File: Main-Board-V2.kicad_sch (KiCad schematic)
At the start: 12 parts, among them IC1 REG1117-5, J4 1-776163-5, U1 OPA325IDBVR, U2 Teensy4.0

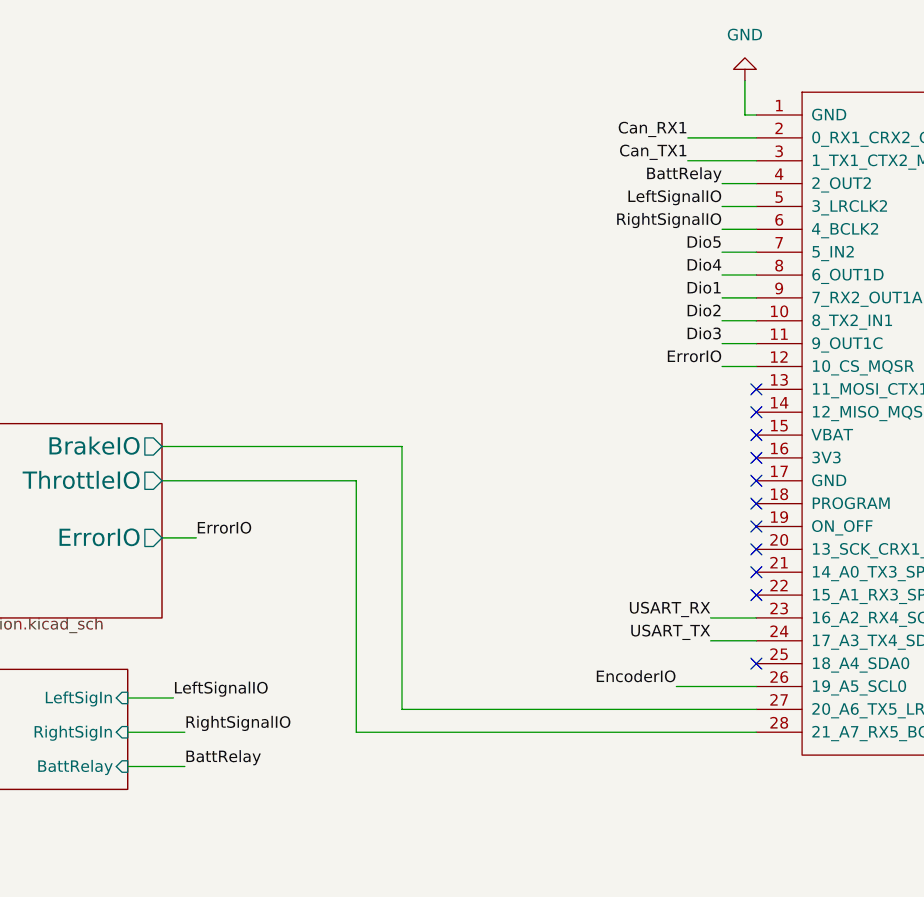
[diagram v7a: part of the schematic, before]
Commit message: finished re-routing, only silkscreen errors left
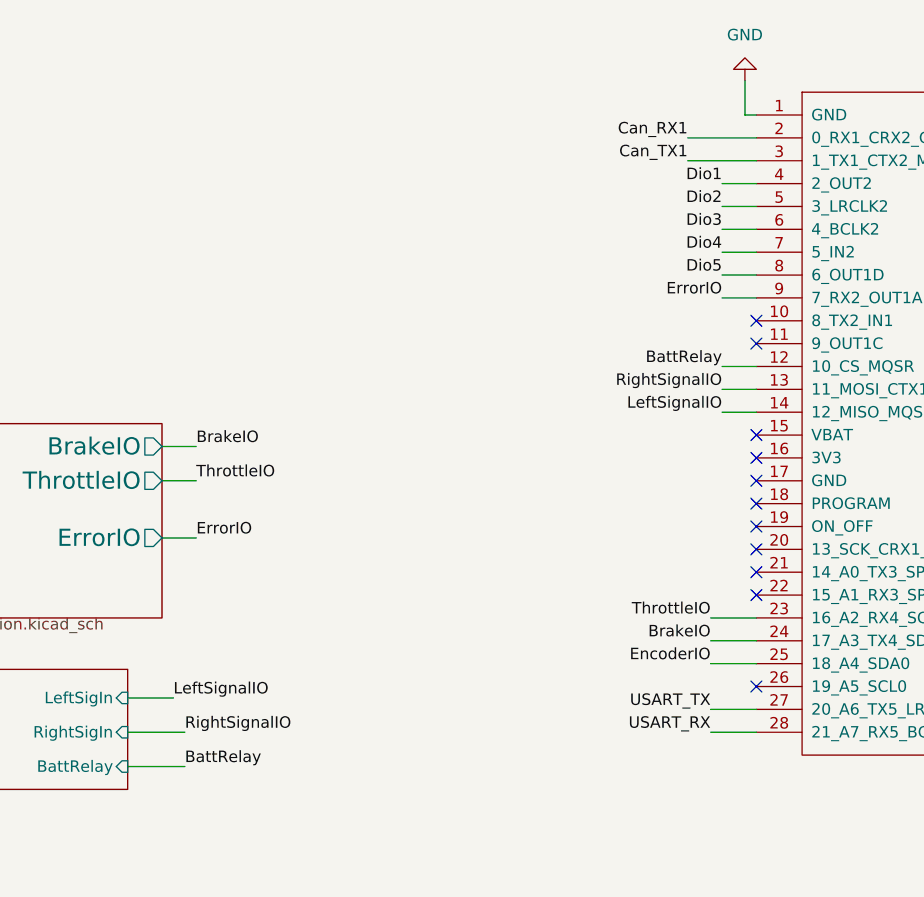
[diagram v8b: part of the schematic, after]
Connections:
- net Pedal/BrakeIO is gone; now on net USART_TX: U2.27 (20_A6_TX5_LRCLK1)
- net Pedal/ThrottleIO is gone; now on net USART_RX: U2.28 (21_A7_RX5_BCLK1)
- net BattRelay: now also U2.12 (10_CS_MQSR); no longer U2.4 (2_OUT2)
- net Dio1: now also U2.4 (2_OUT2); no longer U2.9 (7_RX2_OUT1A)
- net Dio2: now also U2.5 (3_LRCLK2); no longer U2.10 (8_TX2_IN1)
- net Dio3: now also U2.6 (4_BCLK2); no longer U2.11 (9_OUT1C)
- net Dio4: now also U2.7 (5_IN2); no longer U2.8 (6_OUT1D)
- net Dio5: now also U2.8 (6_OUT1D); no longer U2.7 (5_IN2)
- net EncoderIO: now also U2.25 (18_A4_SDA0); no longer U2.26 (19_A5_SCL0)
- net ErrorIO: now also U2.9 (7_RX2_OUT1A); no longer U2.12 (10_CS_MQSR)
- net LeftSignalIO: now also U2.14 (12_MISO_MQSL); no longer U2.5 (3_LRCLK2)
- net RightSignalIO: now also U2.13 (11_MOSI_CTX1); no longer U2.6 (4_BCLK2)
- net USART_RX: no longer U2.23 (16_A2_RX4_SCL1)
- net USART_TX: no longer U2.24 (17_A3_TX4_SDA1)
- new net BrakeIO: U2.24 (17_A3_TX4_SDA1)
- new net ThrottleIO: U2.23 (16_A2_RX4_SCL1)
